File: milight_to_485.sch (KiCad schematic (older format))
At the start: 13 parts

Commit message: upd
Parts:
- added C?: 100nF, Capacitors_SMD:C_0805, symbol C_Cer_SMD_0805
- added C? (x2): 10uF, Capacitors_SMD:C_1206, symbol C_Cer_SMD_1206
- added C?: 1uF, Capacitors_SMD:C_1206, symbol C_Cer_SMD_1206
- added P?: CONN_01X02, symbol CONN_01X02
- added U?: HT7333-A, TO_SOT_Packages_SMD:SOT89-3_Housing, symbol HT7333-A
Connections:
- net labels added: +3.3V, VIN
- wire segments 46 -> 55
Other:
- moved on the sheet: U?

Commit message: upd
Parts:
- added C3, C5: 100n, Capacitors_SMD:C_0805, symbol C_Cer_SMD_0805
- added C4: 1uF, Capacitors_SMD:C_0805, symbol C_Cer_SMD_0805
- added D1: SS13, Diodes_SMD:SMA_Standard, symbol SS13
- added J2: RJ45, Connect:RJ45_8, symbol RJ45
- added U4: 74HC245, Housings_SSOP:TSSOP-20_4.4x6.5mm_Pitch0.65mm, symbol 74HC245
- J1: renamed from J?; footprint (none) -> Connect:RJ12_E
- P1: renamed from P?; footprint (none) -> Pin_Headers:Pin_Header_Straight_1x04
- P2: renamed from P?; footprint (none) -> Pin_Headers:Pin_Header_Straight_1x02
- SW1: renamed from SW?; footprint (none) -> Buttons_Switches_SMD:SW_SPST_FSMSM
- U5: renamed from U?; footprint TO-252 -> TO_SOT_Packages_SMD:TO-252-2Lead
- gave numbers to parts that had none: 14
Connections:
- net labels added: PWM1, PWM1_3, PWM1_4, PWM2, PWM2_1, PWM2_2, PWM2_3, PWM3, PWM4, PWM5
- wire segments 55 -> 91
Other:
- moved on the sheet: C6, R1, R2, R3, SW1, U3

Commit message: PCB update
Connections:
- wire segments 91 -> 95
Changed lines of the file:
@@
 Wire Wire Line
 	2350 6250 1850 6250
+Wire Wire Line
+	9900 4800 9750 4800
+Wire Wire Line
+	9750 4800 9750 5100
+Wire Wire Line
+	9750 5100 9150 5100
+Wire Wire Line
+	9150 5100 9150 4950
+$Comp
+L +5V #PWR030
+U 1 1 56E6CCB7
+P 9150 4950
+F 0 "#PWR030" H 9150 4800 50  0001 C CNN
+F 1 "+5V" H 9150 5090 50  0000 C CNN
+F 2 "" H 9150 4950 50  0000 C CNN
+F 3 "" H 9150 4950 50  0000 C CNN
+	1    9150 4950
+	1    0    0    -1
+$EndComp
 $EndSCHEMATC

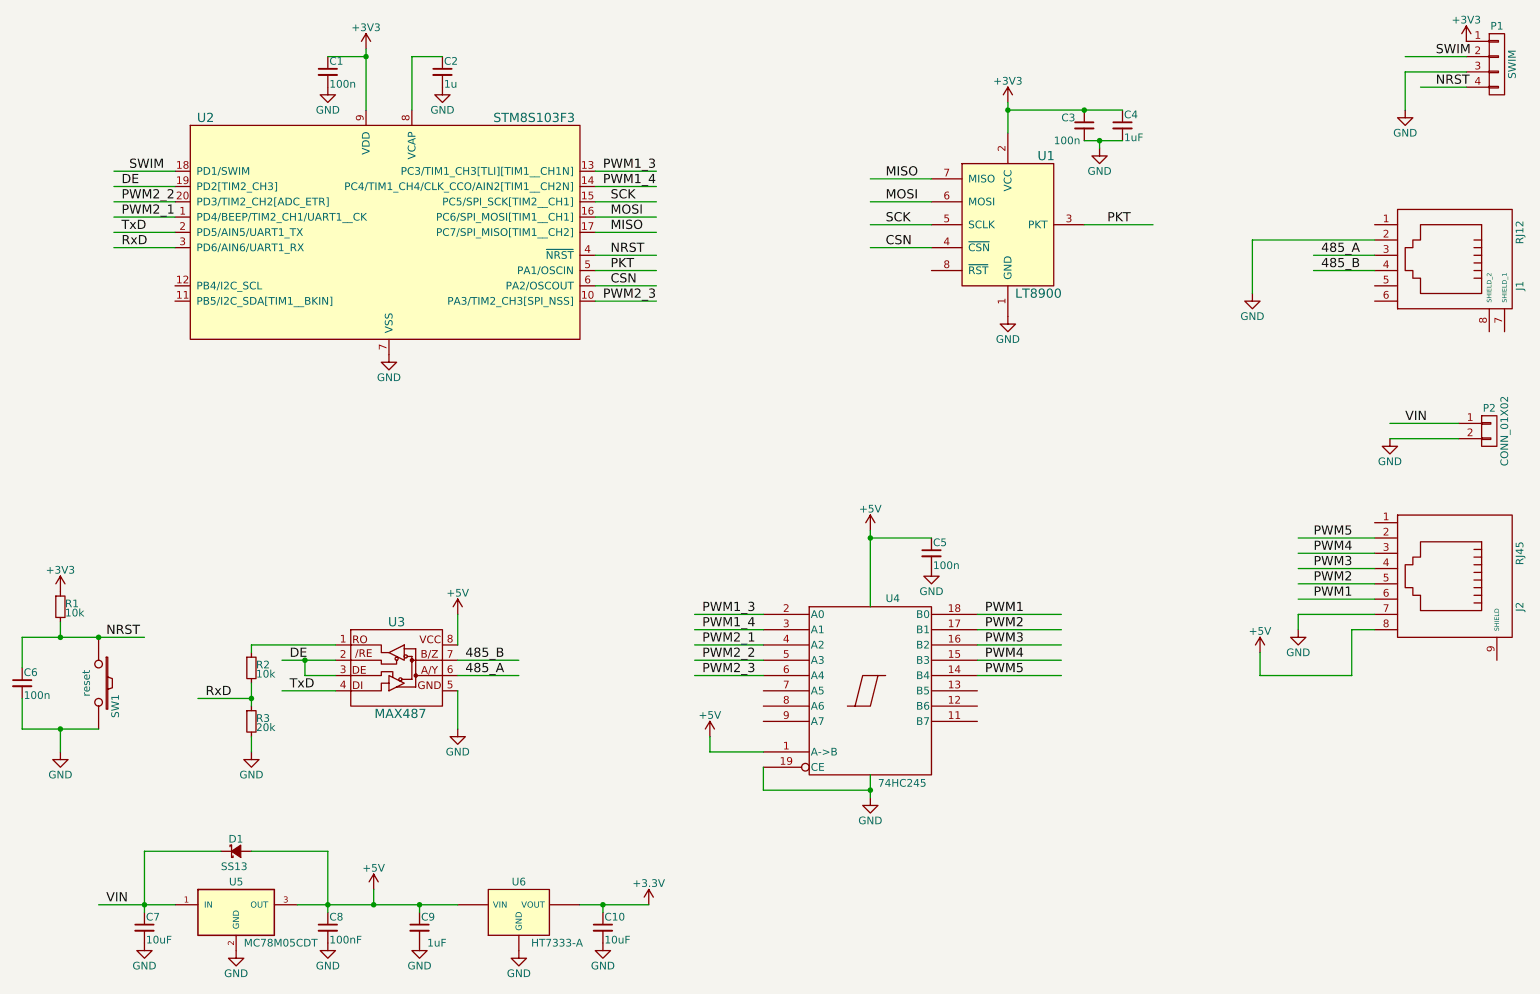
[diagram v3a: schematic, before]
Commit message: PCB Update TTL Output Added
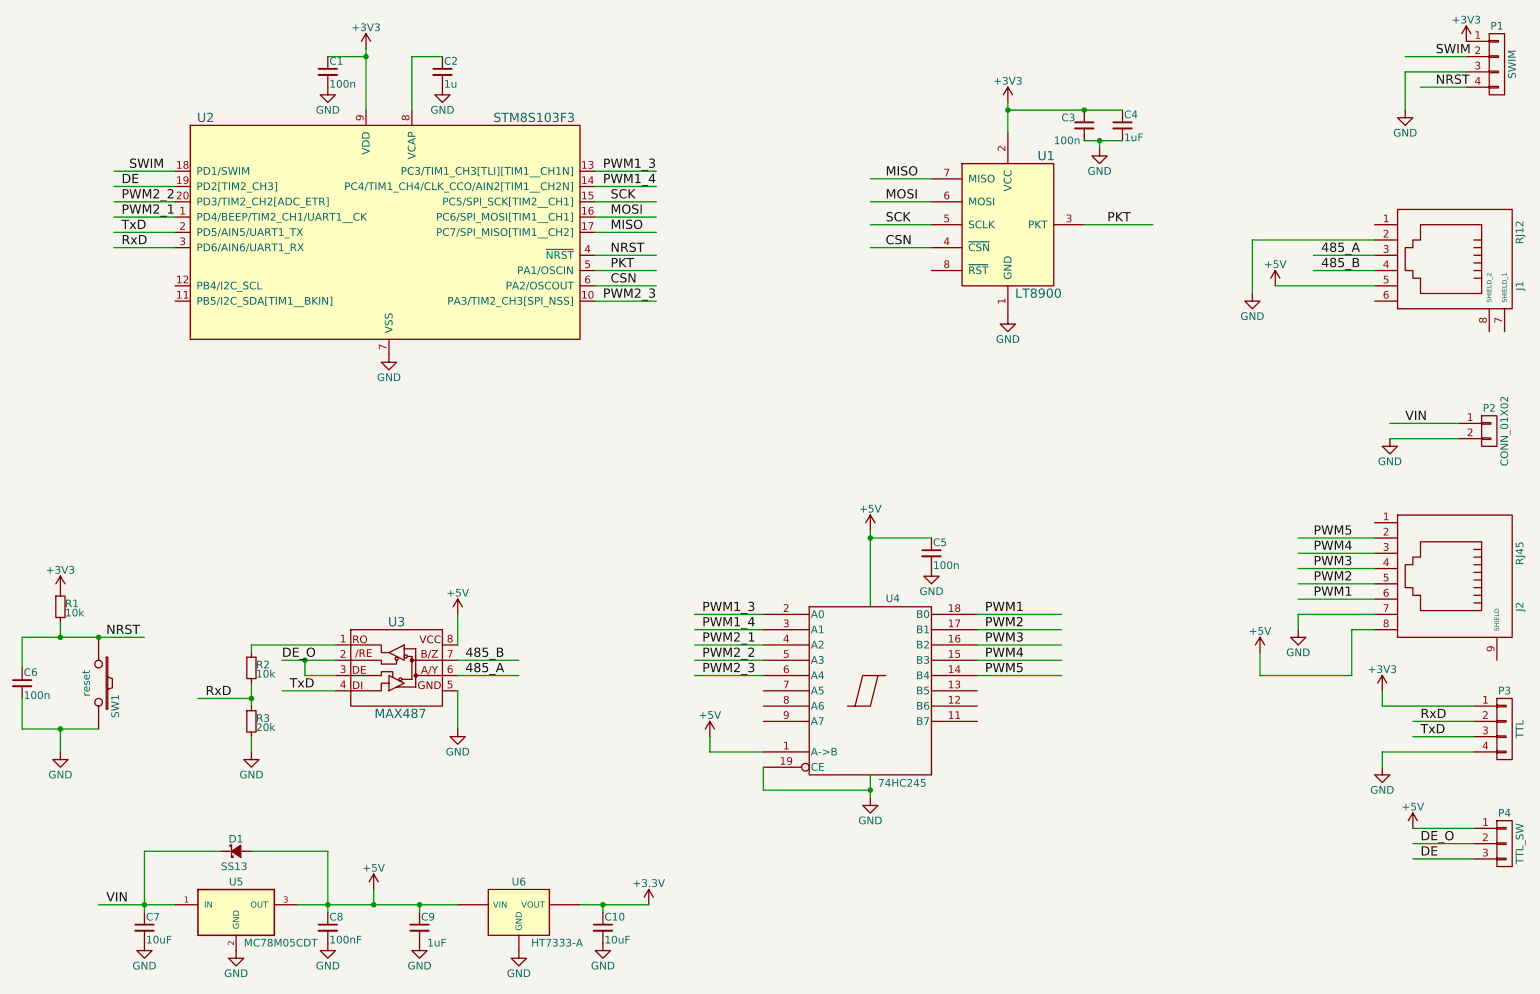
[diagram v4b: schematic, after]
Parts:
- added P3: TTL, Pin_Headers:Pin_Header_Straight_1x04, symbol CONN_01X04
- added P4: TTL_SW, Pin_Headers:Pin_Header_Straight_1x03, symbol CONN_01X03
- J1: footprint Connect:RJ12_E -> BK_Common:RJ12_2mm_Pitch
- J2: footprint Connect:RJ45_8 -> BK_Common:RJ45_UnShielded
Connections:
- net labels added: DE_O
- wire segments 95 -> 105
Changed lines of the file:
@@
 	1    0    0    -1
 $EndComp
-Text Label 2800 5000 0    60   ~ 0
-DE
 Text Label 2250 5250 0    60   ~ 0
 RxD
@@
 F 0 "J1" H 10550 2850 50  0000 C CNN
 F 1 "RJ12" H 10200 2850 50  0000 C CNN
-F 2 "Connect:RJ12_E" H 10350 2350 50  0001 C CNN
+F 2 "BK_Common:RJ12_2mm_Pitch" H 10350 2350 50  0001 C CNN
 F 3 "" H 10350 2350 50  0000 C CNN
 	1    10350 2350
@@
 F 0 "J2" H 10550 4950 50  0000 C CNN
 F 1 "RJ45" H 10200 4950 50  0000 C CNN
-F 2 "Connect:RJ45_8" H 10350 4450 50  0001 C CNN
+F 2 "BK_Common:RJ45_UnShielded" H 10350 4450 50  0001 C CNN
 F 3 "" H 10350 4450 50  0000 C CNN
 	1    10350 4450
@@
 	1    0    0    -1
 $EndComp
+$Comp
+L CONN_01X04 P3
+U 1 1 56E79925
+P 10750 5450
+F 0 "P3" H 10750 5700 50  0000 C CNN
+F 1 "TTL" V 10850 5450 50  0000 C CNN
+F 2 "Pin_Headers:Pin_Header_Straight_1x04" H 10750 5450 50  0001 C CNN
+F 3 "" H 10750 5450 50  0000 C CNN
+	1    10750 5450
+	1    0    0    -1
+$EndComp
+Wire Wire Line
+	10550 5300 9950 5300
+Wire Wire Line
+	9950 5300 9950 5200
+Wire Wire Line
+	10550 5400 10150 5400
+Wire Wire Line
+	10550 5500 10150 5500
+Wire Wire Line
+	10550 5600 9950 5600
+Wire Wire Line
+	9950 5600 9950 5700
+$Comp
+L GND #PWR031
+U 1 1 56E79D7A
+P 9950 5700
+F 0 "#PWR031" H 9950 5450 50  0001 C CNN
+F 1 "GND" H 9950 5550 50  0000 C CNN
+F 2 "" H 9950 5700 50  0000 C CNN
+F 3 "" H 9950 5700 50  0000 C CNN
+	1    9950 5700
+	1    0    0    -1
+$EndComp
+$Comp
+L +3V3 #PWR032
+U 1 1 56E7A543
+P 9950 5200
+F 0 "#PWR032" H 9950 5050 50  0001 C CNN
+F 1 "+3V3" H 9950 5340 50  0000 C CNN
+F 2 "" H 9950 5200 50  0000 C CNN
+F 3 "" H 9950 5200 50  0000 C CNN
+	1    9950 5200
+	1    0    0    -1
+$EndComp
+Text Label 10200 5400 0    60   ~ 0
+RxD
+Text Label 10200 5500 0    60   ~ 0
+TxD
+$Comp
+L +5V #PWR033
+U 1 1 56E7C07B
+P 9250 2550
+F 0 "#PWR033" H 9250 2400 50  0001 C CNN
+F 1 "+5V" H 9250 2690 50  0000 C CNN
+F 2 "" H 9250 2550 50  0000 C CNN
+F 3 "" H 9250 2550 50  0000 C CNN
+	1    9250 2550
+	1    0    0    -1
+$EndComp
+Wire Wire Line
+	9900 2550 9250 2550
+$Comp
+L CONN_01X03 P4
+U 1 1 56E7AD35
+P 10750 6200
+F 0 "P4" H 10750 6400 50  0000 C CNN
+F 1 "TTL_SW" V 10850 6200 50  0000 C CNN
+F 2 "Pin_Headers:Pin_Header_Straight_1x03" H 10750 6200 50  0001 C CNN
+F 3 "" H 10750 6200 50  0000 C CNN
+	1    10750 6200
+	1    0    0    -1
+$EndComp
+Wire Wire Line
+	10550 6100 10150 6100
+Wire Wire Line
+	10550 6200 10150 6200
+Wire Wire Line
+	10550 6300 10150 6300
+Text Label 10200 6300 0    60   ~ 0
+DE
+$Comp
+L +5V #PWR034
+U 1 1 56E7B84A
+P 10150 6100
+F 0 "#PWR034" H 10150 5950 50  0001 C CNN
+F 1 "+5V" H 10150 6240 50  0000 C CNN
+F 2 "" H 10150 6100 50  0000 C CNN
+F 3 "" H 10150 6100 50  0000 C CNN
+	1    10150 6100
+	1    0    0    -1
+$EndComp
+Text Label 10200 6200 0    60   ~ 0
+DE_O
+Text Label 2750 5000 0    60   ~ 0
+DE_O
 $EndSCHEMATC
